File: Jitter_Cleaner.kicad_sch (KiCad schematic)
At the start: 38 parts, among them T1 TCM2-43X+, T3 TCM2-43X+, U18 SI5394, U20 TLV75733PDBV, U21 TLV75718PDBV, Y1 CX3225SB48000D0FPJC1

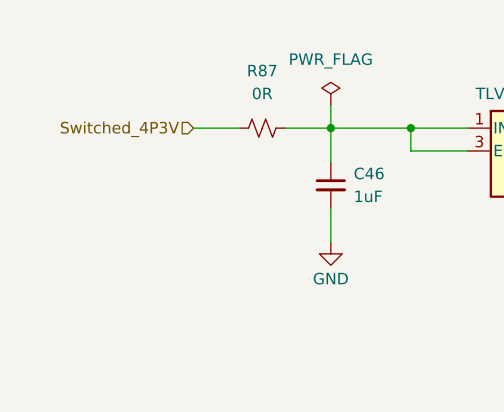
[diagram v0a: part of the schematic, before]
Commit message: Finished Draft Layout
- Finished Draft Layout
- Changed Switcher IC
- Added extra decoupling caps for digital output spikes
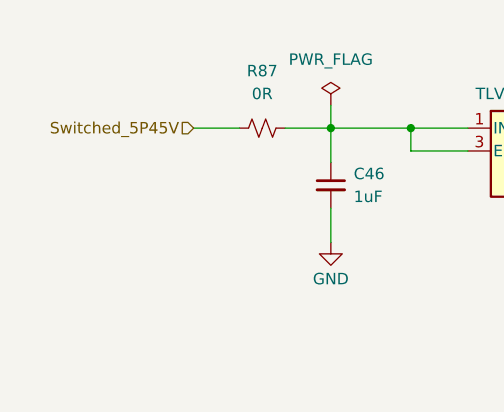
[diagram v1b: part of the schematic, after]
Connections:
- net Switched_4P3V renamed Switched_5P45V
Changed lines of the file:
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@@
 		)
 	)
-	(hierarchical_label "Switched_4P3V"
+	(hierarchical_label "Switched_5P45V"
 		(shape input)
 		(at 55.88 50.8 180)

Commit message: Fixed Silkscreen and BOM
All DRC/ERC errors are resolved.
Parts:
- C17, C18, C19, C20, C21, C22, C23, C24, C25, C26, C27, C28, C29, C55, C57, C59, C60: Digikey (none) -> 490-14514-6-ND
- C46: Comment CAP CER 1UF 16V X7R 0603 -> (none); Designator C6 -> (none); Digikey (none) -> 490-5241-6-ND; LCSC C161212 -> (none)
- C47: Comment CAP CER 1UF 16V X7R 0603 -> (none); Designator C8 -> (none); Digikey (none) -> 490-5241-6-ND; LCSC C161212 -> (none)
- C50, C63, C73: Comment CAP CER 10UF 25V X5R 0805 -> (none); Designator C7 -> (none); Digikey (none) -> 490-5523-6-ND; LCSC C84416 -> (none)
- C51: Comment CAP CER 10UF 25V X5R 0805 -> (none); Designator C9 -> (none); Digikey (none) -> 490-5523-6-ND; LCSC C84416 -> (none)
- CLK1, CLK2: Digikey (none) -> SAM10617-ND
- R60: Digikey (none) -> 311-100LRDKR-ND
- R62, R64: Digikey (none) -> RG16P100BDKR-ND
- R86, R87: Digikey (none) -> P0.0GDKR-ND
- T1, T3: Digikey (none) -> 3157-TCM2-43X+DKR-ND
- TP5: Comment Red PC Test Point, Miniature Phosphor Bronze Silver Plating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 -> (none); Designator TP5 -> (none); Digikey (none) -> 36-5000-ND; LCSC C5199900 -> (none)
- TP7: Comment Red PC Test Point, Miniature Phosphor Bronze Silver Plating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 -> (none); Designator TP4 -> (none); Digikey (none) -> 36-5000-ND; LCSC C5199900 -> (none)
- U18: Digikey (none) -> 336-4800-ND
- U20: Digikey (none) -> 296-50414-6-ND
- U21: Digikey (none) -> 296-50413-6-ND
- Y1: Digikey (none) -> 478-CX3225SB48000D0FPJC1DKR-ND

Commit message: Final Draft for project
- Changed LDO for Digital Output driver to a LP3855-ADJ
- Aligned Digital Output driver sections
- Added Additional Capacitance on each digital output drive channel
- Revised Differential Lines geometry on top layer
- Revised Power routing and internal planes
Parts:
- C17, C18, C19, C20, C21, C22, C23, C24, C25, C26, C27, C28, C29, C55, C57, C59, C60: Digikey 490-14514-6-ND -> (none)
- C46, C47: Digikey 490-5241-6-ND -> (none)
- C50, C51, C63, C73: Digikey 490-5523-6-ND -> (none)
- CLK1, CLK2: Digikey SAM10617-ND -> (none)
- R60: Digikey 311-100LRDKR-ND -> (none)
- R62, R64: Digikey RG16P100BDKR-ND -> (none)
- R86, R87: Digikey P0.0GDKR-ND -> (none)
- T1, T3: Digikey 3157-TCM2-43X+DKR-ND -> (none)
- TP5, TP7: Digikey 36-5000-ND -> (none)
- U18: Digikey 336-4800-ND -> (none)
- U20: Digikey 296-50414-6-ND -> (none)
- U21: Digikey 296-50413-6-ND -> (none)
- Y1: Digikey 478-CX3225SB48000D0FPJC1DKR-ND -> (none)

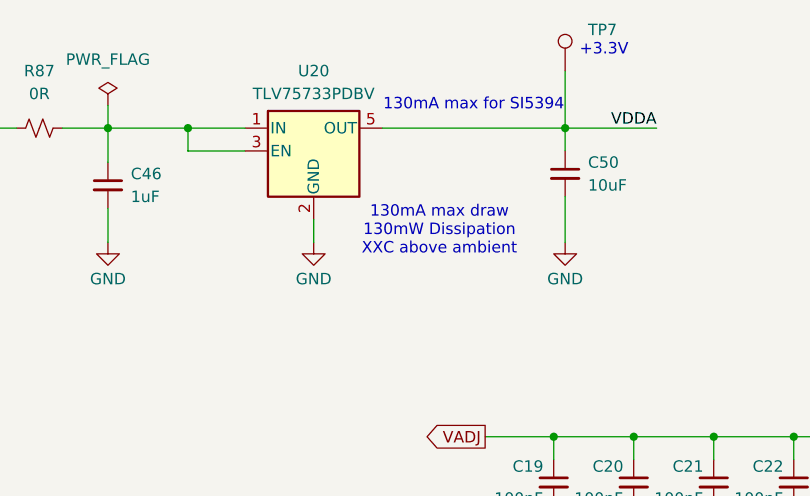
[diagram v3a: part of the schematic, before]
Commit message: Schematic and Layout Tweaks
- Updated all vias to 0.6/0.3mm
- New mechanical universal Marble holes for H2
- widen the power traces to Test points
- Add pin 4 of U20/U24 to GND net
- add a GND pour around U44 for heat
- Widen GND traces on LDOs (U24/U20)
- Grounding of unused gates of level shifters
-Small updates footprints for U18,U19,U23,U25
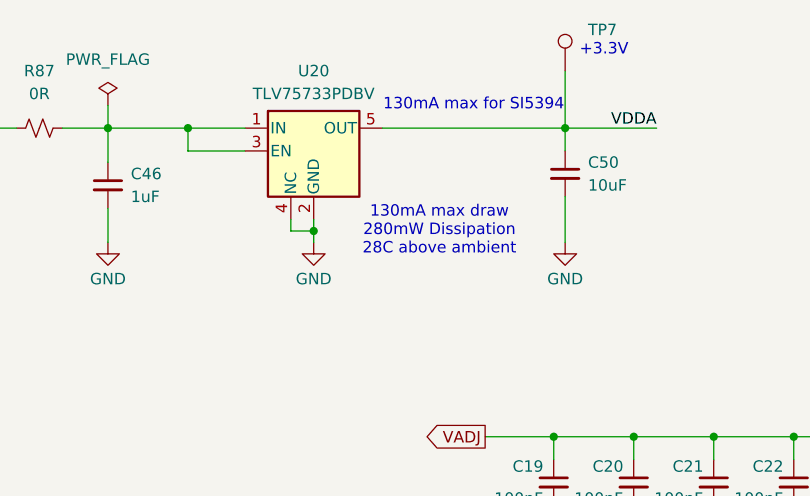
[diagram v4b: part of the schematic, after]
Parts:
- U20: symbol Regulator_Linear:TLV75733PDBV -> evr-fmc:TLV7xxxx_SOT23-5
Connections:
- net GND: now also U20.4 (NC)
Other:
- note added: "130mA max draw 280mW Dissipation 28C above ambient"
- note removed: "130mA max draw 130mW Dissipation XXC above ambient"
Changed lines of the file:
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@@
 		(members "OE" "SDI" "SDO" "CLK" "CS")
 	)
-	(text "130mA max draw\n130mW Dissipation\nXXC above ambient"
+	(text "130mA max draw\n280mW Dissipation\n28C above ambient"
 		(exclude_from_sim no)
 		(at 107.95 62.23 0)
@@
 	)
 	(junction
+		(at 93.98 62.23)
+		(diameter 0)
+		(color 0 0 0 0)
+	)
+	(junction
 		(at 182.88 50.8)
 		(diameter 0)
@@
 	(wire
 		(pts
+			(xy 93.98 62.23) (xy 93.98 63.5)
+		)
+		(stroke
+			(width 0)
+			(type default)
+		)
+	)
+	(wire
+		(pts
 			(xy 193.04 241.3) (xy 186.69 241.3)
 		)
@@
 	(wire
 		(pts
+			(xy 91.44 62.23) (xy 93.98 62.23)
+		)
+		(stroke
+			(width 0)
+			(type default)
+		)
+	)
+	(wire
+		(pts
 			(xy 187.96 85.09) (xy 187.96 87.63)
 		)
@@
 	(wire
 		(pts
-			(xy 93.98 60.96) (xy 93.98 63.5)
+			(xy 93.98 60.96) (xy 93.98 62.23)
 		)
 		(stroke
@@
 	(wire
 		(pts
+			(xy 91.44 60.96) (xy 91.44 62.23)
+		)
+		(stroke
+			(width 0)
+			(type default)
+		)
+	)
+	(wire
+		(pts
 			(xy 104.14 123.19) (xy 104.14 125.73)
 		)
@@
 	)
 	(symbol
-		(lib_id "Regulator_Linear:TLV75733PDBV")
+		(lib_id "evr-fmc:TLV7xxxx_SOT23-5")
 		(at 93.98 53.34 0)
 		(unit 1)

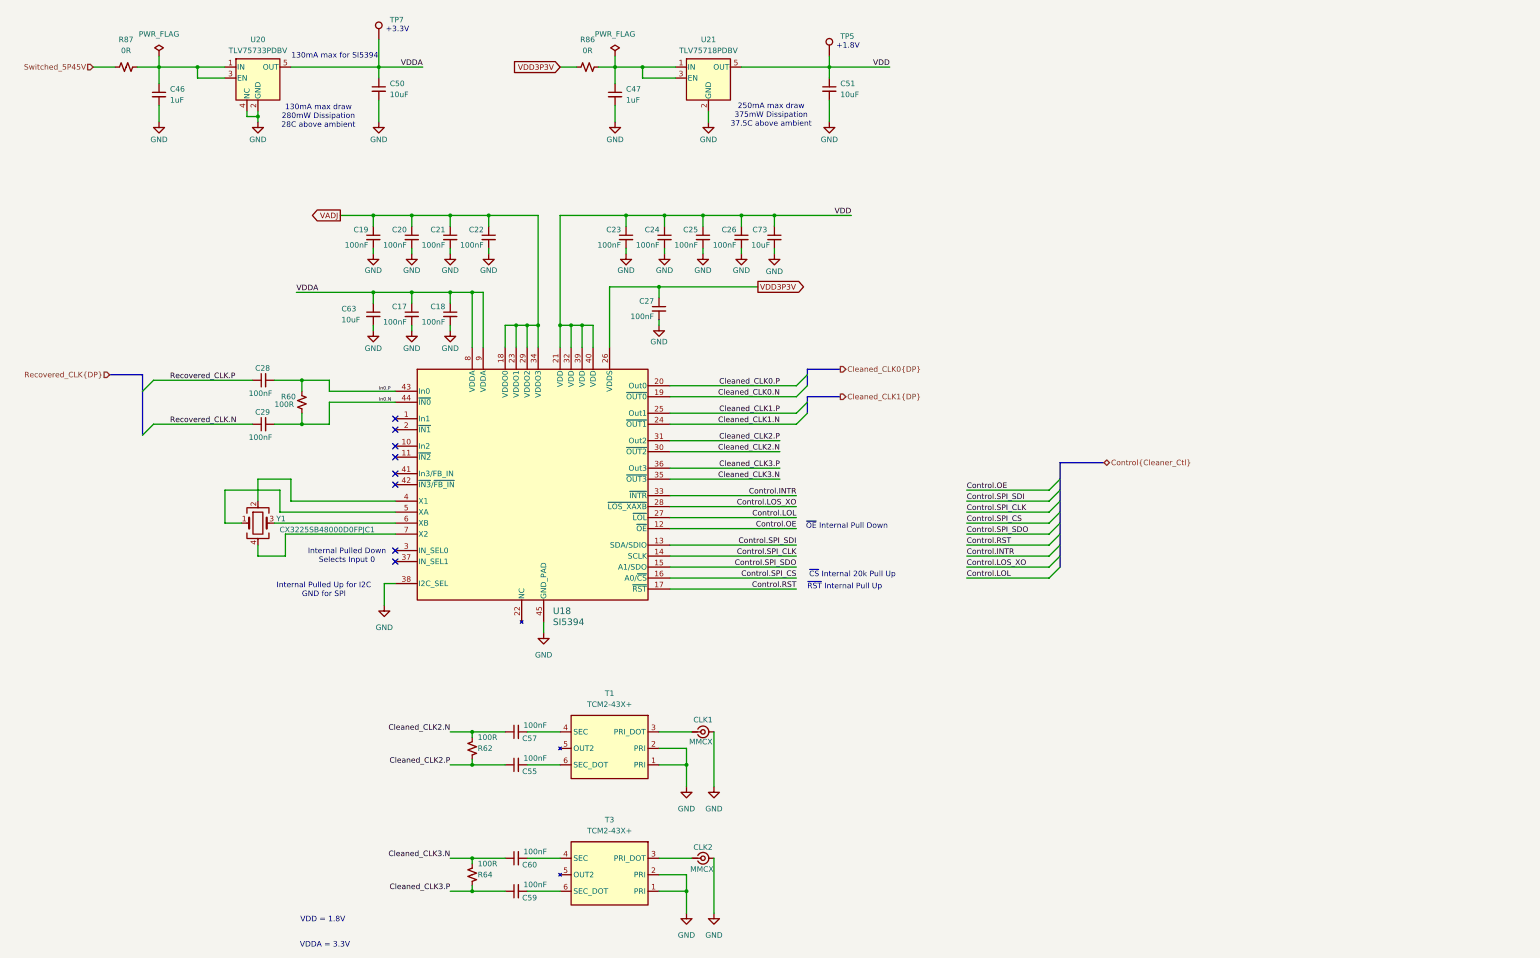
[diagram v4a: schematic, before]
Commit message: Updated Layout of XOs and Digital Output Sections
- Added some additional comments to schematics (Y1&Y2)
- Added additional ground vias around U44
- Add GND planes around 1.8V LDOs (U21&U28)
- Straightened out some power routing tracks with 90deg bends
- Revised routing of Y1&Y2
- Revised routing of each digital output section
- All DCR/ERC errors resolved.
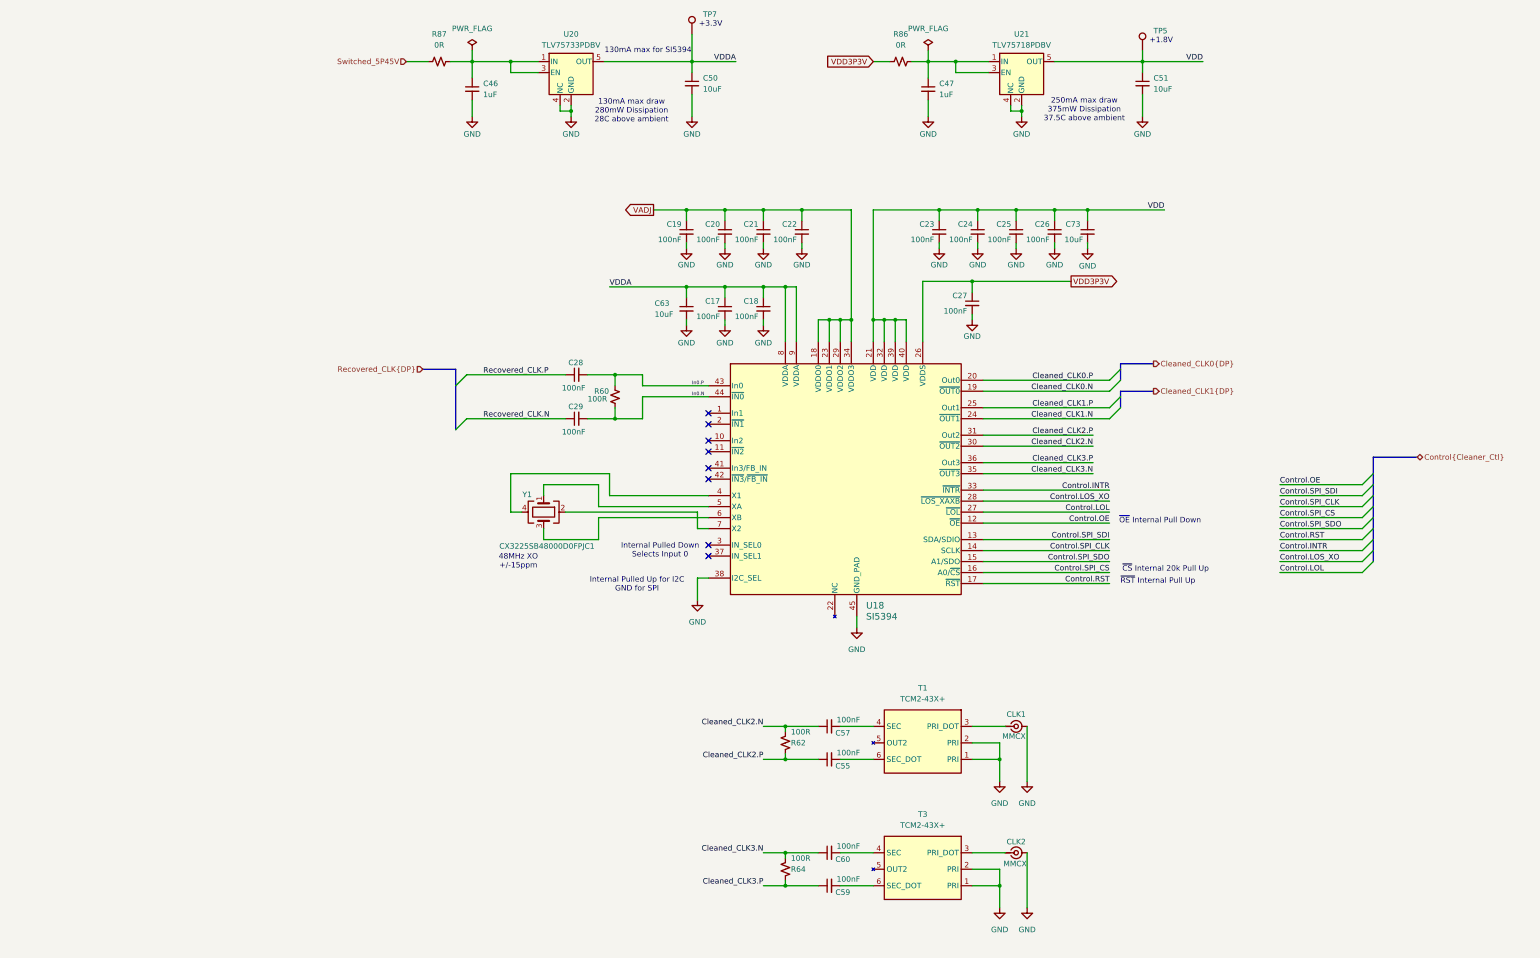
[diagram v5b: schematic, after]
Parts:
- U21: symbol Regulator_Linear:TLV75718PDBV -> evr-fmc:TLV7xxxx_SOT23-5
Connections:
- net GND: now also U21.4 (NC)
- net at U18.4 (X1): now also Y1.4; no longer Y1.2
- net at U18.7 (X2): now also Y1.2; no longer Y1.4
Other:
- note added: "48MHz XO +/-15ppm"
- note removed: "VDD = 1.8V"
- note removed: "VDDA = 3.3V"
- moved on the sheet: C17, C18, C19, C20, C21, C22, C23, C24, C25, C26, C27, C28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
